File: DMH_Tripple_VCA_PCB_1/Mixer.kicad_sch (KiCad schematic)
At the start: 8 parts, among them U2 TL074

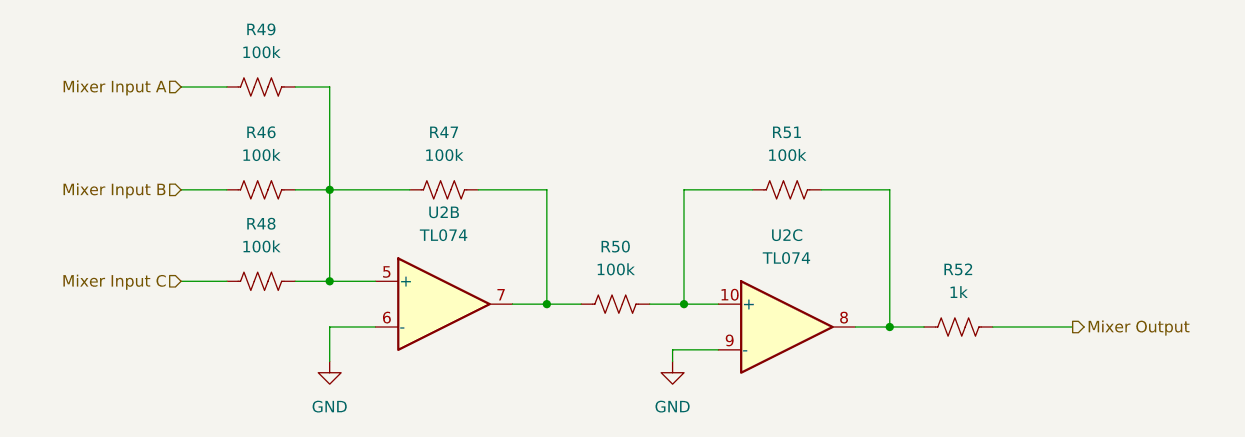
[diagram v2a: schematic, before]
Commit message: PCB 1 component positioning in progress
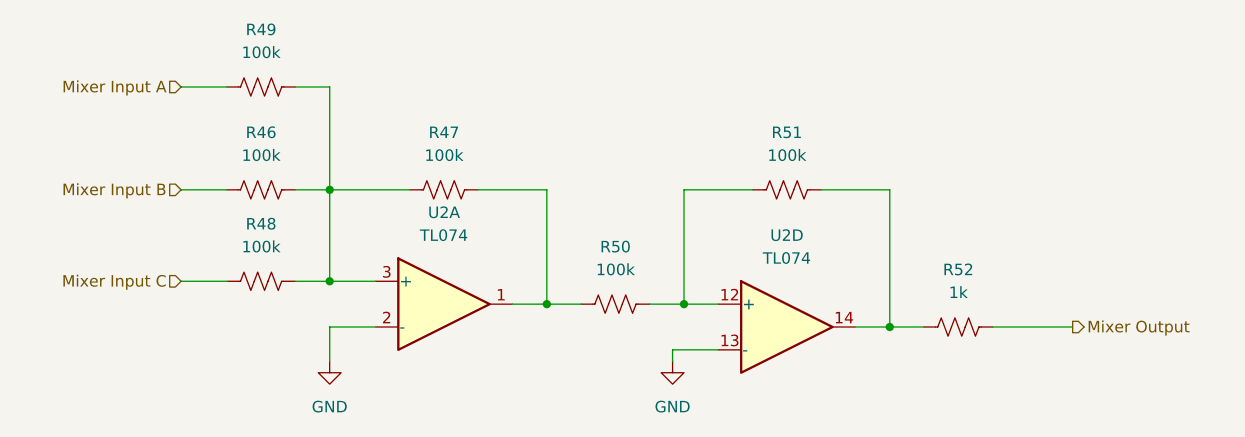
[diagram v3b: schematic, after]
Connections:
- net GND: now also U2.13 (-), U2.2 (-); no longer U2.6 (-), U2.9 (-)
- net at R46.2, R47.1, R48.2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: now also U2.3 (+); no longer U2.5 (+)
- net at R47.2, R50.1: now also U2.1; no longer U2.7
- net at R50.2, R51.1: now also U2.12 (+); no longer U2.10 (+)
- net at R51.2, R52.1: now also U2.14; no longer U2.8
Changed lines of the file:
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@@
 		(lib_id "Amplifier_Operational:TL074")
 		(at 76.2 88.9 0)
-		(unit 2)
+		(unit 1)
 		(exclude_from_sim no)
 		(in_bom yes)
@@
 				(path "/58f4306d-5387-4983-bb08-41a2313fd315/cf2dec9f-6388-4d4b-9b45-78eb859d2e80"
 					(reference "U2")
-					(unit 2)
+					(unit 1)
 				)
 			)
@@
 		(lib_id "Amplifier_Operational:TL074")
 		(at 114.3 91.44 0)
-		(unit 3)
+		(unit 4)
 		(exclude_from_sim no)
 		(in_bom yes)
@@
 				(path "/58f4306d-5387-4983-bb08-41a2313fd315/cf2dec9f-6388-4d4b-9b45-78eb859d2e80"
 					(reference "U2")
-					(unit 3)
-				)
-			)
+					(unit 4)
+				)
+			)

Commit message: Adjusted OpAmp pinouts for placement
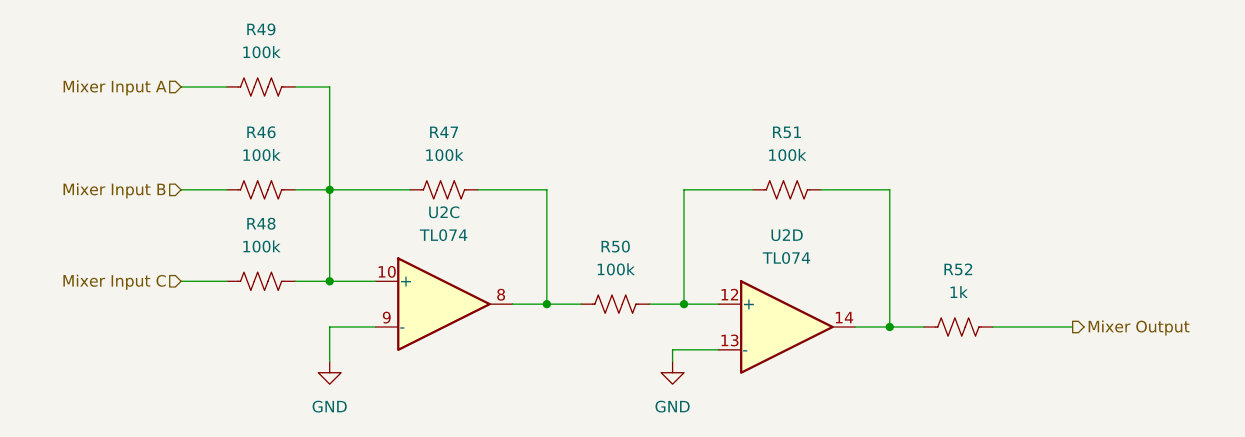
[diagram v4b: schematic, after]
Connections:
- net GND: now also U2.9 (-); no longer U2.2 (-)
- net at R47.2, R50.1: now also U2.8; no longer U2.1
- net at R46.2, R47.1, R48.2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: now also U2.10 (+); no longer U2.3 (+)
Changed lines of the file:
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@@
 		(lib_id "Amplifier_Operational:TL074")
 		(at 76.2 88.9 0)
-		(unit 1)
+		(unit 3)
 		(exclude_from_sim no)
 		(in_bom yes)
@@
 				(path "/58f4306d-5387-4983-bb08-41a2313fd315/cf2dec9f-6388-4d4b-9b45-78eb859d2e80"
 					(reference "U2")
-					(unit 1)
+					(unit 3)
 				)
 			)

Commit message: Started routing over with upright resistor fps
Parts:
- R46, R47, R48, R49, R50, R51, R52: footprint Resistor_THT:R_Axial_DIN0207_L6.3mm_D2.5mm_P7.62mm_Horizontal -> Resistor_THT:R_Axial_DIN0207_L6.3mm_D2.5mm_P2.54mm_Vertical
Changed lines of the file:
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@@
 			)
 		)
-		(property "Footprint" "Resistor_THT:R_Axial_DIN0207_L6.3mm_D2.5mm_P7.62mm_Horizontal"
+		(property "Footprint" "Resistor_THT:R_Axial_DIN0207_L6.3mm_D2.5mm_P2.54mm_Vertical"
 			(at 76.454 75.184 90)
 			(effects
@@
 			)
 		)
-		(property "Footprint" "Resistor_THT:R_Axial_DIN0207_L6.3mm_D2.5mm_P7.62mm_Horizontal"
+		(property "Footprint" "Resistor_THT:R_Axial_DIN0207_L6.3mm_D2.5mm_P2.54mm_Vertical"
 			(at 56.134 63.754 90)
 			(effects
@@
 			)
 		)
-		(property "Footprint" "Resistor_THT:R_Axial_DIN0207_L6.3mm_D2.5mm_P7.62mm_Horizontal"
+		(property "Footprint" "Resistor_THT:R_Axial_DIN0207_L6.3mm_D2.5mm_P2.54mm_Vertical"
 			(at 114.554 75.184 90)
 			(effects
@@
 			)
 		)
-		(property "Footprint" "Resistor_THT:R_Axial_DIN0207_L6.3mm_D2.5mm_P7.62mm_Horizontal"
+		(property "Footprint" "Resistor_THT:R_Axial_DIN0207_L6.3mm_D2.5mm_P2.54mm_Vertical"
 			(at 133.604 90.424 90)
 			(effects
@@
 			)
 		)
-		(property "Footprint" "Resistor_THT:R_Axial_DIN0207_L6.3mm_D2.5mm_P7.62mm_Horizontal"
+		(property "Footprint" "Resistor_THT:R_Axial_DIN0207_L6.3mm_D2.5mm_P2.54mm_Vertical"
 			(at 56.134 75.184 90)
 			(effects
@@
 			)
 		)
-		(property "Footprint" "Resistor_THT:R_Axial_DIN0207_L6.3mm_D2.5mm_P7.62mm_Horizontal"
+		(property "Footprint" "Resistor_THT:R_Axial_DIN0207_L6.3mm_D2.5mm_P2.54mm_Vertical"
 			(at 56.134 85.344 90)
 			(effects
@@
 			)
 		)
-		(property "Footprint" "Resistor_THT:R_Axial_DIN0207_L6.3mm_D2.5mm_P7.62mm_Horizontal"
+		(property "Footprint" "Resistor_THT:R_Axial_DIN0207_L6.3mm_D2.5mm_P2.54mm_Vertical"
 			(at 95.504 87.884 90)
 			(effects
